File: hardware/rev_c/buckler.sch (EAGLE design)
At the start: 90 parts, among them J1 DB25_5747846, J2 DM3AT-SF-PEJM5, J3 GROVE-CONNECTOR-DIP(4P-2.0), J4 GROVE-CONNECTOR-DIP(4P-2.0), J5 GROVE-CONNECTOR-DIP(4P-2.0), J6 GROVE-CONNECTOR-DIP(4P-2.0), J7 NRF52832DK_SHIELD, U1 ADXL327, U2 MAX44009, U3 MPU-9250, U4 MS5637-02BA03, U5 SI7021-A20-GM1, U6 SIP32510

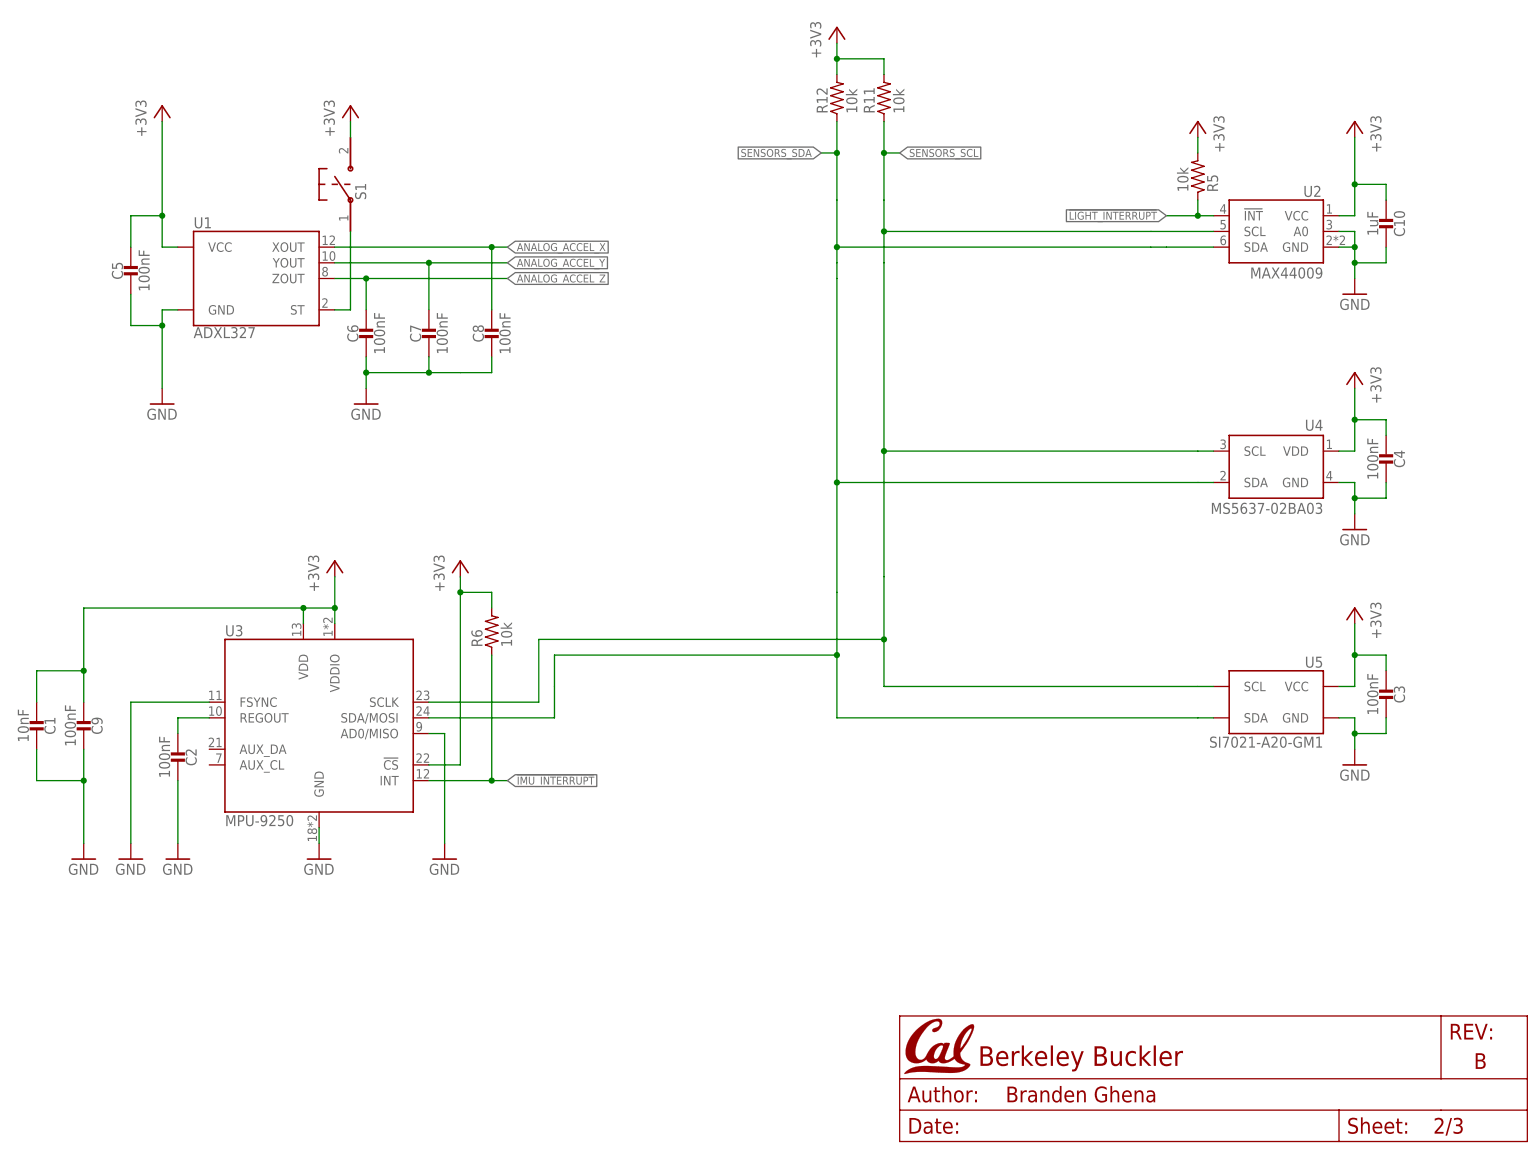
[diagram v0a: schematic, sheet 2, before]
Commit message: Address problems in #2
Reroute light, temp/hum, pressure sensors to make room for IC number
labels. Rename 3v3->VCC. Flip UART RX/TX on DB25 connector. Move gyro
axis label out from under LCD screen.
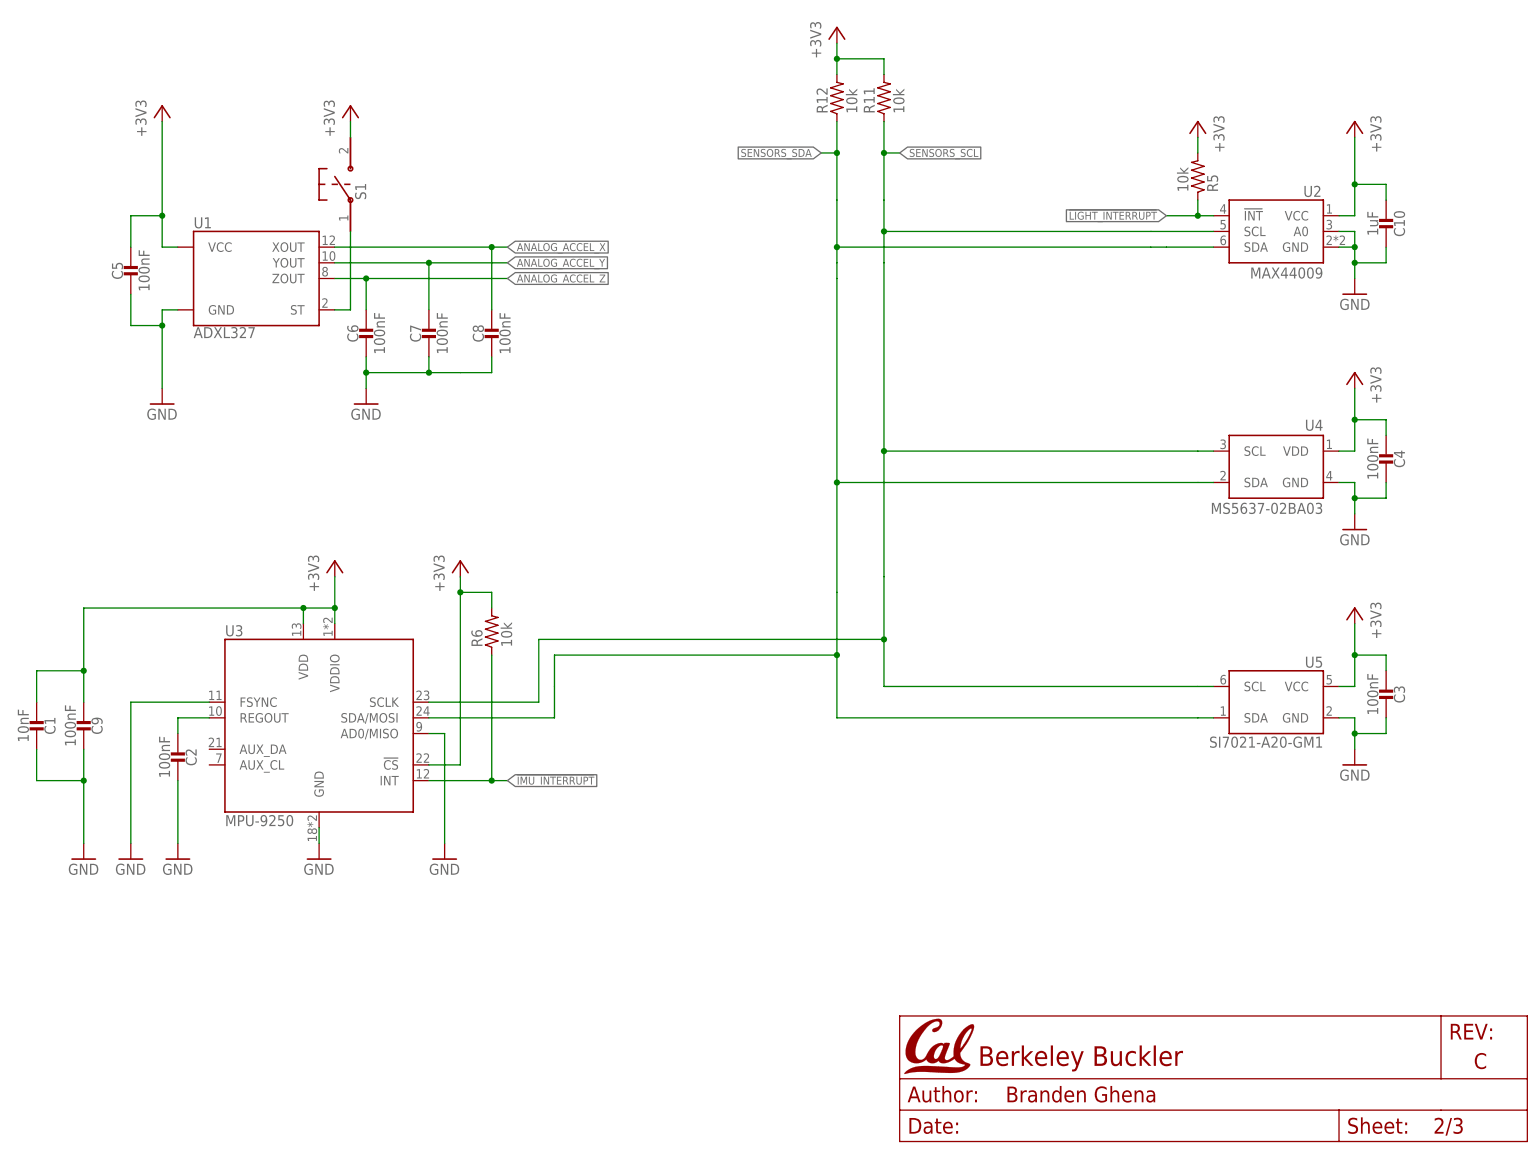
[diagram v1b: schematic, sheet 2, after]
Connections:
- net UART_RX: now also J1.2; no longer J1.1
- net UART_TX: now also J1.1; no longer J1.2

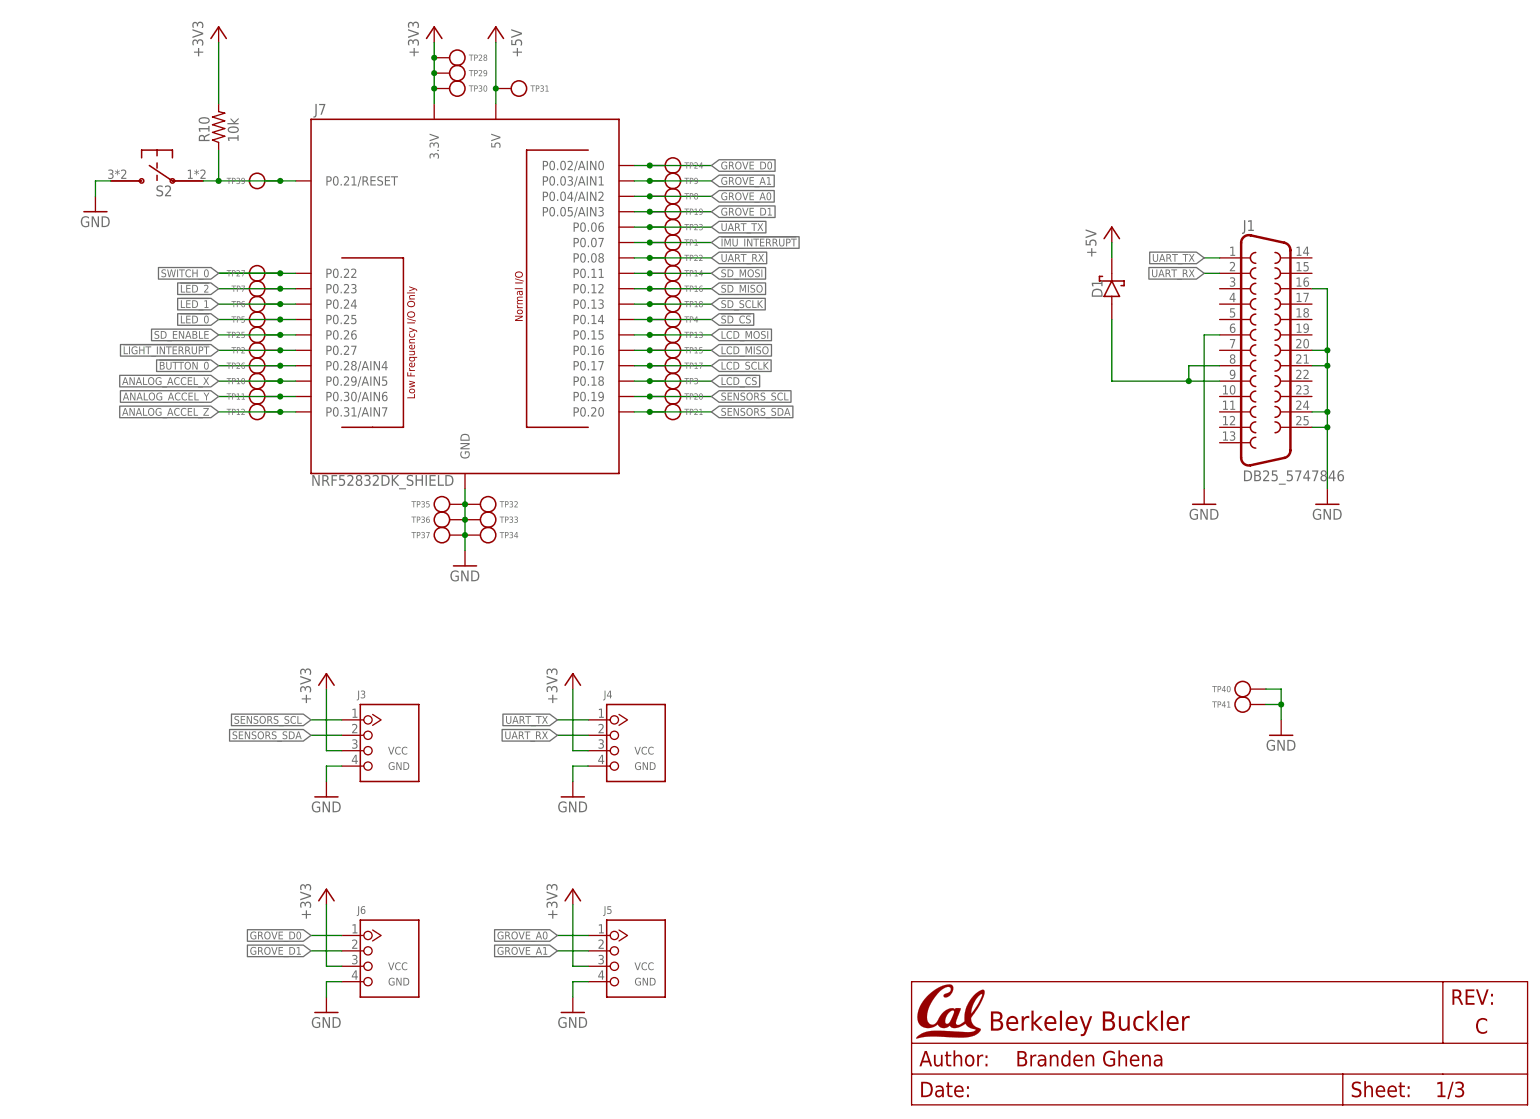
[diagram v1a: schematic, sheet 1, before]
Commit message: Use actual parts instead of test points
Name nrf52dk headers too.
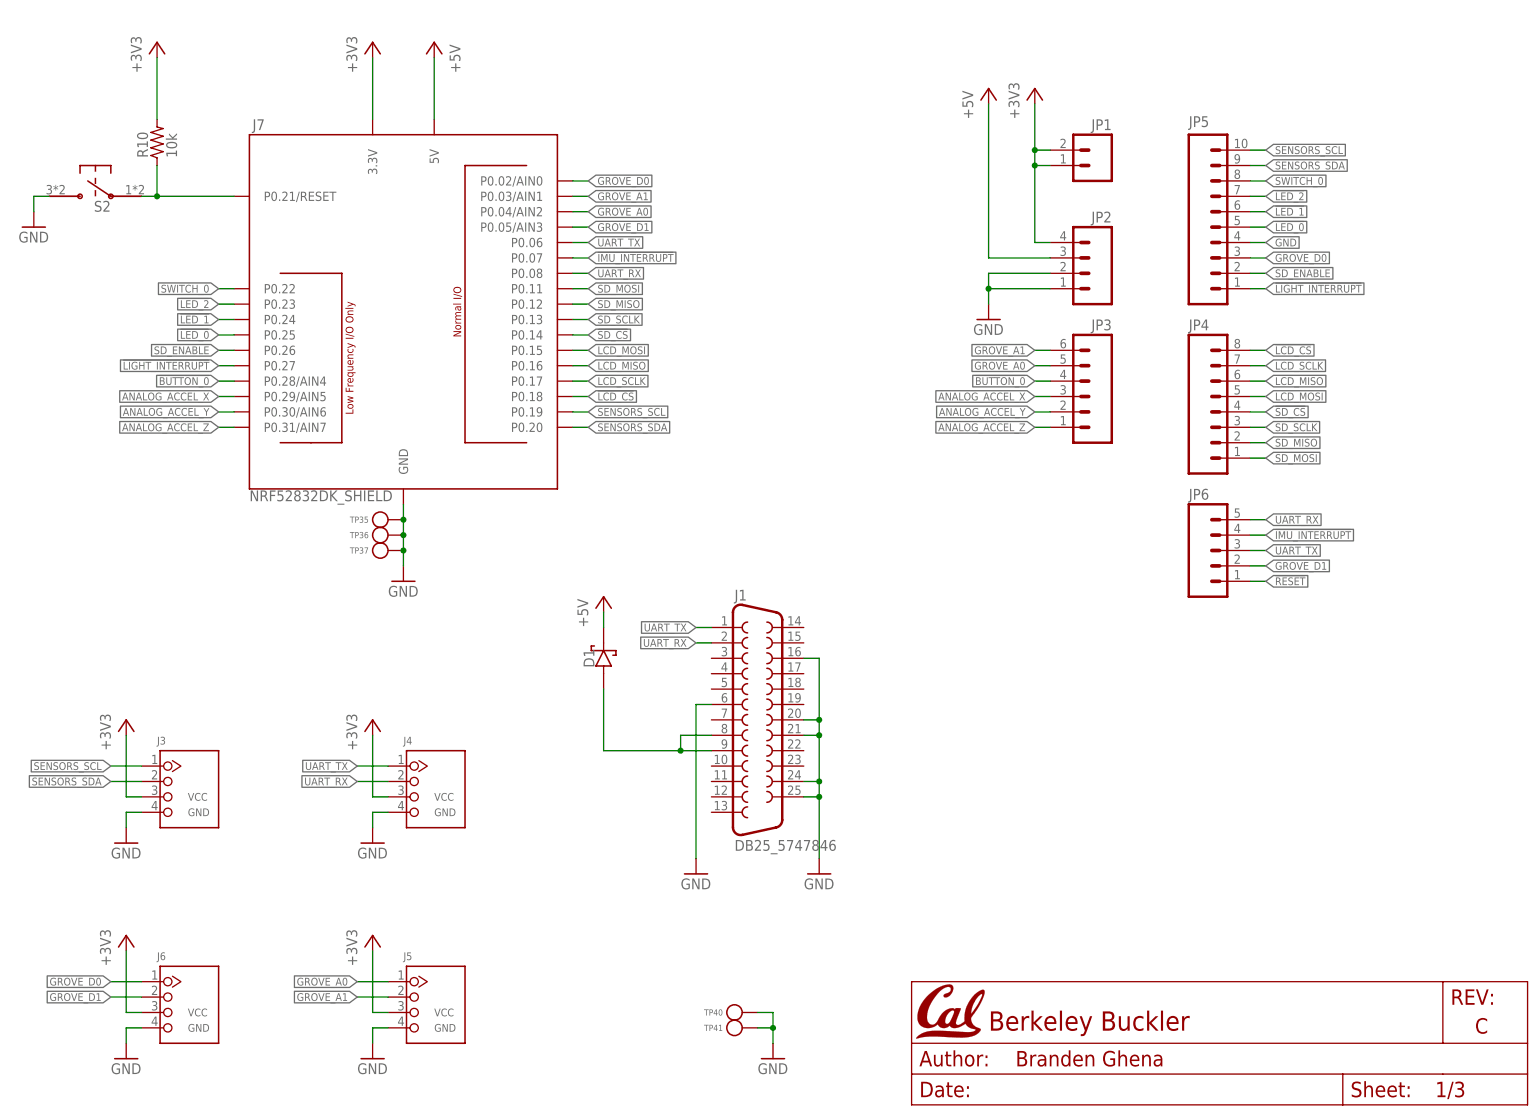
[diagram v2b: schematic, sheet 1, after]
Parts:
- removed TP1, TP10, TP11, TP12, TP13, TP14, TP15, TP16, TP17, TP18, TP19, TP2, TP20, TP21, TP22, TP23, TP24, TP25, TP26, TP27, TP28, TP29, TP3, TP30, TP31, TP32, TP33, TP34, TP39, TP4, TP5, TP6, TP7, TP8, TP9: TEST_POINT_0.040IN, headers:TEST_POINT_0.040IN
- added JP1: (no value), SparkFun-Connectors:M02PTH
- added JP2: (no value), SparkFun-Connectors:M04PTH
- added JP3: (no value), SparkFun-Connectors:M06SIP
- added JP4: (no value), SparkFun-Connectors:M081X08
- added JP5: M10", SparkFun-Connectors:M10"
- added JP6: (no value), SparkFun-Connectors:M05PTH
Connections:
- net !BUTTON_0: now also JP3.4; no longer TP26.TESTPOINT
- net !IMU_INTERRUPT: now also JP6.4; no longer TP1.TESTPOINT
- net !LCD_CS: now also JP4.8; no longer TP3.TESTPOINT
- net !LED_0: now also JP5.5; no longer TP5.TESTPOINT
- net !LED_1: now also JP5.6; no longer TP6.TESTPOINT
- net !LED_2: now also JP5.7; no longer TP7.TESTPOINT
- net !LIGHT_INTERRUPT: now also JP5.1; no longer TP2.TESTPOINT
- net !RESET: now also JP6.1; no longer TP39.TESTPOINT
- net !SD_CS: now also JP4.4; no longer TP4.TESTPOINT
- net +3V3: now also JP1.1, JP1.2, JP2.4; no longer TP28.TESTPOINT, TP29.TESTPOINT, TP30.TESTPOINT
- net +5V: now also JP2.3; no longer TP31.TESTPOINT
- net ANALOG_ACCEL_X: now also JP3.3; no longer TP10.TESTPOINT
- net ANALOG_ACCEL_Y: now also JP3.2; no longer TP11.TESTPOINT
- net ANALOG_ACCEL_Z: now also JP3.1; no longer TP12.TESTPOINT
- net GND: now also JP2.1, JP2.2, JP5.4; no longer TP32.TESTPOINT, TP33.TESTPOINT, TP34.TESTPOINT
- net GROVE_A0: now also JP3.5; no longer TP8.TESTPOINT
- net GROVE_A1: now also JP3.6; no longer TP9.TESTPOINT
- net GROVE_D0: now also JP5.3; no longer TP24.TESTPOINT
- net GROVE_D1: now also JP6.2; no longer TP19.TESTPOINT
- net LCD_MISO: now also JP4.6; no longer TP15.TESTPOINT
- net LCD_MOSI: now also JP4.5; no longer TP13.TESTPOINT
- net LCD_SCLK: now also JP4.7; no longer TP17.TESTPOINT
- net SD_ENABLE: now also JP5.2; no longer TP25.TESTPOINT
- net SD_MISO: now also JP4.2; no longer TP16.TESTPOINT
- net SD_MOSI: now also JP4.1; no longer TP14.TESTPOINT
- net SD_SCLK: now also JP4.3; no longer TP18.TESTPOINT
- net SENSORS_SCL: now also JP5.10; no longer TP20.TESTPOINT
- net SENSORS_SDA: now also JP5.9; no longer TP21.TESTPOINT
- net SWITCH_0: now also JP5.8; no longer TP27.TESTPOINT
- net UART_RX: now also JP6.5; no longer TP22.TESTPOINT
- net UART_TX: now also JP6.3; no longer TP23.TESTPOINT
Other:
- note added: "Expansion Headers"
- moved on the sheet: D1, J1, J3, J4, J5, J6, J7, R10, S2, TP35, TP36, TP37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
